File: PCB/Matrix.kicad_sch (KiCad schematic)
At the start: 67 parts, among them SW1 CPG151101S11, SW10 CPG151101S11, SW11 CPG151101S11, SW12 CPG151101S11, SW13 CPG151101S11, SW14 CPG151101S11, SW15 CPG151101S11, SW16 CPG151101S11, SW17 CPG151101S11, SW18 CPG151101S11, SW19 CPG151101S11, SW2 CPG151101S11, SW20 CPG151101S11, SW21 CPG151101S11, SW22 CPG151101S11, SW23 CPG151101S11, SW24 CPG151101S11, SW25 CPG151101S11, SW26 CPG151101S11, SW27 CPG151101S11, SW28 CPG151101S11, SW29 CPG151101S11, SW3 CPG151101S11, SW30 CPG151101S11, SW31 Encoder, SW4 CPG151101S11, SW5 CPG151101S11, SW6 CPG151101S11, SW7 CPG151101S11, SW8 CPG151101S11, SW9 CPG151101S11

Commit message: More routing
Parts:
- SW1, SW10, SW11, SW12, SW13, SW14, SW15, SW16, SW17, SW18, SW19, SW2, SW20, SW21, SW22, SW23, SW24, SW25, SW26, SW27, SW28, SW29, SW3, SW30, SW4, SW5, SW6, SW7, SW8, SW9: footprint Cantaloupe:MX_1U-Hotswap-Dual -> Cantaloupe:MX_1U-Hotswap-Flippable
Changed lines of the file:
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@@
       (effects (font (size 1.524 1.524)) hide)
     )
-    (property "Footprint" "Cantaloupe:MX_1U-Hotswap-Dual" (at 66.04 77.47 0)
+    (property "Footprint" "Cantaloupe:MX_1U-Hotswap-Flippable" (at 66.04 77.47 0)
       (effects (font (size 1.524 1.524)) hide)
     )
@@
       (effects (font (size 1.524 1.524)) hide)
     )
-    (property "Footprint" "Cantaloupe:MX_1U-Hotswap-Dual" (at 66.04 46.99 0)
+    (property "Footprint" "Cantaloupe:MX_1U-Hotswap-Flippable" (at 66.04 46.99 0)
       (effects (font (size 1.524 1.524)) hide)
     )
@@
       (effects (font (size 1.524 1.524)) hide)
     )
-    (property "Footprint" "Cantaloupe:MX_1U-Hotswap-Dual" (at 40.64 31.75 0)
+    (property "Footprint" "Cantaloupe:MX_1U-Hotswap-Flippable" (at 40.64 31.75 0)
       (effects (font (size 1.524 1.524)) hide)
     )
@@
       (effects (font (size 1.524 1.524)) hide)
     )
-    (property "Footprint" "Cantaloupe:MX_1U-Hotswap-Dual" (at 27.94 77.47 0)
+    (property "Footprint" "Cantaloupe:MX_1U-Hotswap-Flippable" (at 27.94 77.47 0)
       (effects (font (size 1.524 1.524)) hide)
     )
@@
       (effects (font (size 1.524 1.524)) hide)
     )
-    (property "Footprint" "Cantaloupe:MX_1U-Hotswap-Dual" (at 53.34 62.23 0)
+    (property "Footprint" "Cantaloupe:MX_1U-Hotswap-Flippable" (at 53.34 62.23 0)
       (effects (font (size 1.524 1.524)) hide)
     )
@@
       (effects (font (size 1.524 1.524)) hide)
     )
-    (property "Footprint" "Cantaloupe:MX_1U-Hotswap-Dual" (at 27.94 31.75 0)
+    (property "Footprint" "Cantaloupe:MX_1U-Hotswap-Flippable" (at 27.94 31.75 0)
       (effects (font (size 1.524 1.524)) hide)
     )
@@
       (effects (font (size 1.524 1.524)) hide)
     )
-    (property "Footprint" "Cantaloupe:MX_1U-Hotswap-Dual" (at 40.64 46.99 0)
+    (property "Footprint" "Cantaloupe:MX_1U-Hotswap-Flippable" (at 40.64 46.99 0)
       (effects (font (size 1.524 1.524)) hide)
     )
@@
       (effects (font (size 1.524 1.524)) hide)
     )
-    (property "Footprint" "Cantaloupe:MX_1U-Hotswap-Dual" (at 40.64 62.23 0)
+    (property "Footprint" "Cantaloupe:MX_1U-Hotswap-Flippable" (at 40.64 62.23 0)
       (effects (font (size 1.524 1.524)) hide)
     )
@@
       (effects (font (size 1.524 1.524)) hide)
     )
-    (property "Footprint" "Cantaloupe:MX_1U-Hotswap-Dual" (at 91.44 46.99 0)
+    (property "Footprint" "Cantaloupe:MX_1U-Hotswap-Flippable" (at 91.44 46.99 0)
       (effects (font (size 1.524 1.524)) hide)
     )
@@
       (effects (font (size 1.524 1.524)) hide)
     )
-    (property "Footprint" "Cantaloupe:MX_1U-Hotswap-Dual" (at 53.34 16.51 0)
+    (property "Footprint" "Cantaloupe:MX_1U-Hotswap-Flippable" (at 53.34 16.51 0)
       (effects (font (size 1.524 1.524)) hide)
     )
@@
       (effects (font (size 1.524 1.524)) hide)
     )
-    (property "Footprint" "Cantaloupe:MX_1U-Hotswap-Dual" (at 27.94 16.51 0)
+    (property "Footprint" "Cantaloupe:MX_1U-Hotswap-Flippable" (at 27.94 16.51 0)
       (effects (font (size 1.524 1.524)) hide)
     )
@@
       (effects (font (size 1.524 1.524)) hide)
     )
-    (property "Footprint" "Cantaloupe:MX_1U-Hotswap-Dual" (at 53.34 46.99 0)
+    (property "Footprint" "Cantaloupe:MX_1U-Hotswap-Flippable" (at 53.34 46.99 0)
       (effects (font (size 1.524 1.524)) hide)
     )
@@
       (effects (font (size 1.524 1.524)) hide)
     )
-    (property "Footprint" "Cantaloupe:MX_1U-Hotswap-Dual" (at 66.04 31.75 0)
+    (property "Footprint" "Cantaloupe:MX_1U-Hotswap-Flippable" (at 66.04 31.75 0)
       (effects (font (size 1.524 1.524)) hide)
     )
@@
       (effects (font (size 1.524 1.524)) hide)
     )
-    (property "Footprint" "Cantaloupe:MX_1U-Hotswap-Dual" (at 78.74 46.99 0)
+    (property "Footprint" "Cantaloupe:MX_1U-Hotswap-Flippable" (at 78.74 46.99 0)
       (effects (font (size 1.524 1.524)) hide)
     )
@@
       (effects (font (size 1.524 1.524)) hide)
     )
-    (property "Footprint" "Cantaloupe:MX_1U-Hotswap-Dual" (at 78.74 77.47 0)
+    (property "Footprint" "Cantaloupe:MX_1U-Hotswap-Flippable" (at 78.74 77.47 0)
       (effects (font (size 1.524 1.524)) hide)
     )
@@
       (effects (font (size 1.524 1.524)) hide)
     )
-    (property "Footprint" "Cantaloupe:MX_1U-Hotswap-Dual" (at 53.34 31.75 0)
+    (property "Footprint" "Cantaloupe:MX_1U-Hotswap-Flippable" (at 53.34 31.75 0)
       (effects (font (size 1.524 1.524)) hide)
     )
@@
       (effects (font (size 1.524 1.524)) hide)
     )
-    (property "Footprint" "Cantaloupe:MX_1U-Hotswap-Dual" (at 91.44 31.75 0)
+    (property "Footprint" "Cantaloupe:MX_1U-Hotswap-Flippable" (at 91.44 31.75 0)
       (effects (font (size 1.524 1.524)) hide)
     )
@@
       (effects (font (size 1.524 1.524)) hide)
     )
-    (property "Footprint" "Cantaloupe:MX_1U-Hotswap-Dual" (at 66.04 62.23 0)
+    (property "Footprint" "Cantaloupe:MX_1U-Hotswap-Flippable" (at 66.04 62.23 0)
       (effects (font (size 1.524 1.524)) hide)
     )
@@
       (effects (font (size 1.524 1.524)) hide)
     )
-    (property "Footprint" "Cantaloupe:MX_1U-Hotswap-Dual" (at 27.94 46.99 0)
+    (property "Footprint" "Cantaloupe:MX_1U-Hotswap-Flippable" (at 27.94 46.99 0)
       (effects (font (size 1.524 1.524)) hide)
     )
@@
       (effects (font (size 1.524 1.524)) hide)
     )
-    (property "Footprint" "Cantaloupe:MX_1U-Hotswap-Dual" (at 40.64 16.51 0)
+    (property "Footprint" "Cantaloupe:MX_1U-Hotswap-Flippable" (at 40.64 16.51 0)
       (effects (font (size 1.524 1.524)) hide)
     )
@@
       (effects (font (size 1.524 1.524)) hide)
     )
-    (property "Footprint" "Cantaloupe:MX_1U-Hotswap-Dual" (at 53.34 77.47 0)
+    (property "Footprint" "Cantaloupe:MX_1U-Hotswap-Flippable" (at 53.34 77.47 0)
       (effects (font (size 1.524 1.524)) hide)
     )
@@
       (effects (font (size 1.524 1.524)) hide)
     )
-    (property "Footprint" "Cantaloupe:MX_1U-Hotswap-Dual" (at 78.74 31.75 0)
+    (property "Footprint" "Cantaloupe:MX_1U-Hotswap-Flippable" (at 78.74 31.75 0)
       (effects (font (size 1.524 1.524)) hide)
     )
@@
       (effects (font (size 1.524 1.524)) hide)
     )
-    (property "Footprint" "Cantaloupe:MX_1U-Hotswap-Dual" (at 78.74 62.23 0)
+    (property "Footprint" "Cantaloupe:MX_1U-Hotswap-Flippable" (at 78.74 62.23 0)
       (effects (font (size 1.524 1.524)) hide)
     )
@@
       (effects (font (size 1.524 1.524)) hide)
     )
-    (property "Footprint" "Cantaloupe:MX_1U-Hotswap-Dual" (at 27.94 62.23 0)
+    (property "Footprint" "Cantaloupe:MX_1U-Hotswap-Flippable" (at 27.94 62.23 0)
       (effects (font (size 1.524 1.524)) hide)
     )
@@
       (effects (font (size 1.524 1.524)) hide)
     )
-    (property "Footprint" "Cantaloupe:MX_1U-Hotswap-Dual" (at 91.44 62.23 0)
+    (property "Footprint" "Cantaloupe:MX_1U-Hotswap-Flippable" (at 91.44 62.23 0)
       (effects (font (size 1.524 1.524)) hide)
     )
@@
       (effects (font (size 1.524 1.524)) hide)
     )
-    (property "Footprint" "Cantaloupe:MX_1U-Hotswap-Dual" (at 91.44 77.47 0)
+    (property "Footprint" "Cantaloupe:MX_1U-Hotswap-Flippable" (at 91.44 77.47 0)
       (effects (font (size 1.524 1.524)) hide)
     )
@@
       (effects (font (size 1.524 1.524)) hide)
     )
-    (property "Footprint" "Cantaloupe:MX_1U-Hotswap-Dual" (at 78.74 16.51 0)
+    (property "Footprint" "Cantaloupe:MX_1U-Hotswap-Flippable" (at 78.74 16.51 0)
       (effects (font (size 1.524 1.524)) hide)
     )
@@
       (effects (font (size 1.524 1.524)) hide)
     )
-    (property "Footprint" "Cantaloupe:MX_1U-Hotswap-Dual" (at 40.64 77.47 0)
+    (property "Footprint" "Cantaloupe:MX_1U-Hotswap-Flippable" (at 40.64 77.47 0)
       (effects (font (size 1.524 1.524)) hide)
     )
@@
       (effects (font (size 1.524 1.524)) hide)
     )
-    (property "Footprint" "Cantaloupe:MX_1U-Hotswap-Dual" (at 66.04 16.51 0)
+    (property "Footprint" "Cantaloupe:MX_1U-Hotswap-Flippable" (at 66.04 16.51 0)
       (effects (font (size 1.524 1.524)) hide)
     )
@@
       (effects (font (size 1.524 1.524)) hide)
     )
-    (property "Footprint" "Cantaloupe:MX_1U-Hotswap-Dual" (at 91.44 16.51 0)
-      (effects (font (size 1.524 1.524)) hide)
-    )
+    (property "Footprint" "Cantaloupe:MX_1U-Hotswap-Flippable" (at 91.44 16.51 0)
+      (effects (font (size 1.524 1.524)) hide)
+    )

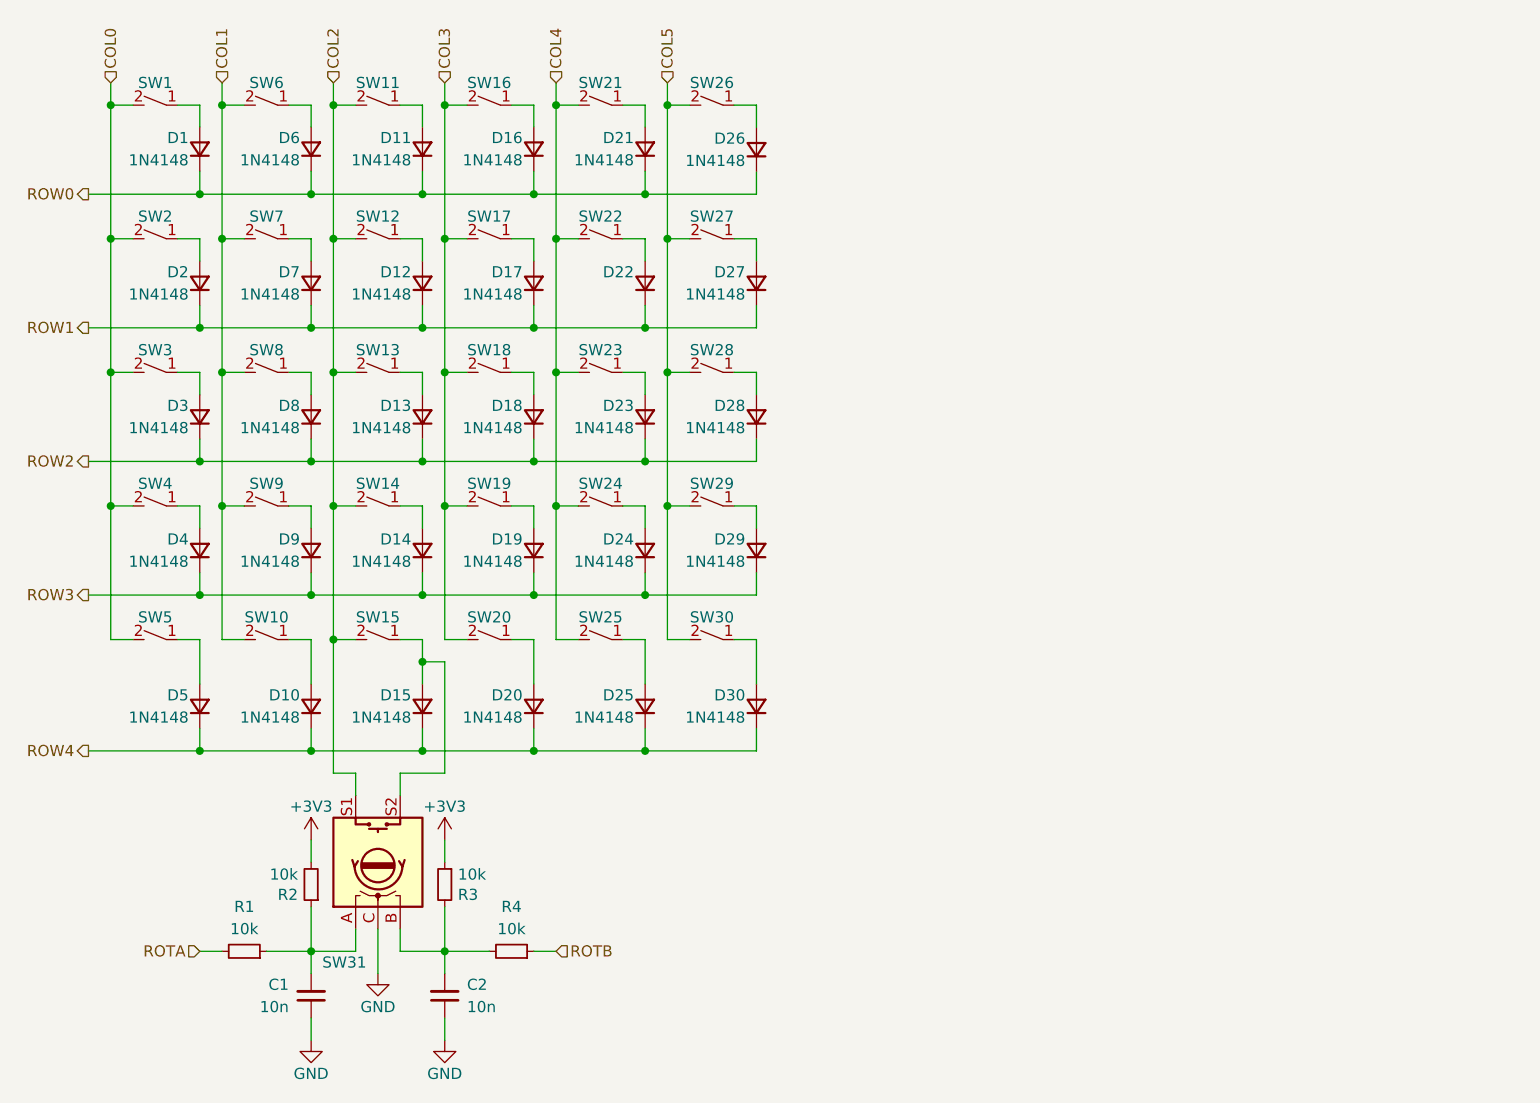
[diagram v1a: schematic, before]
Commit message: 08/08/2023 update
Removed Ogen footprint, and future VIK support is planned. Rerouted board following latest Honeydew revision. WIP support for the USB2541 is added, but it's very tentative and not yet complete. Added CX70M-24P1 footprint.
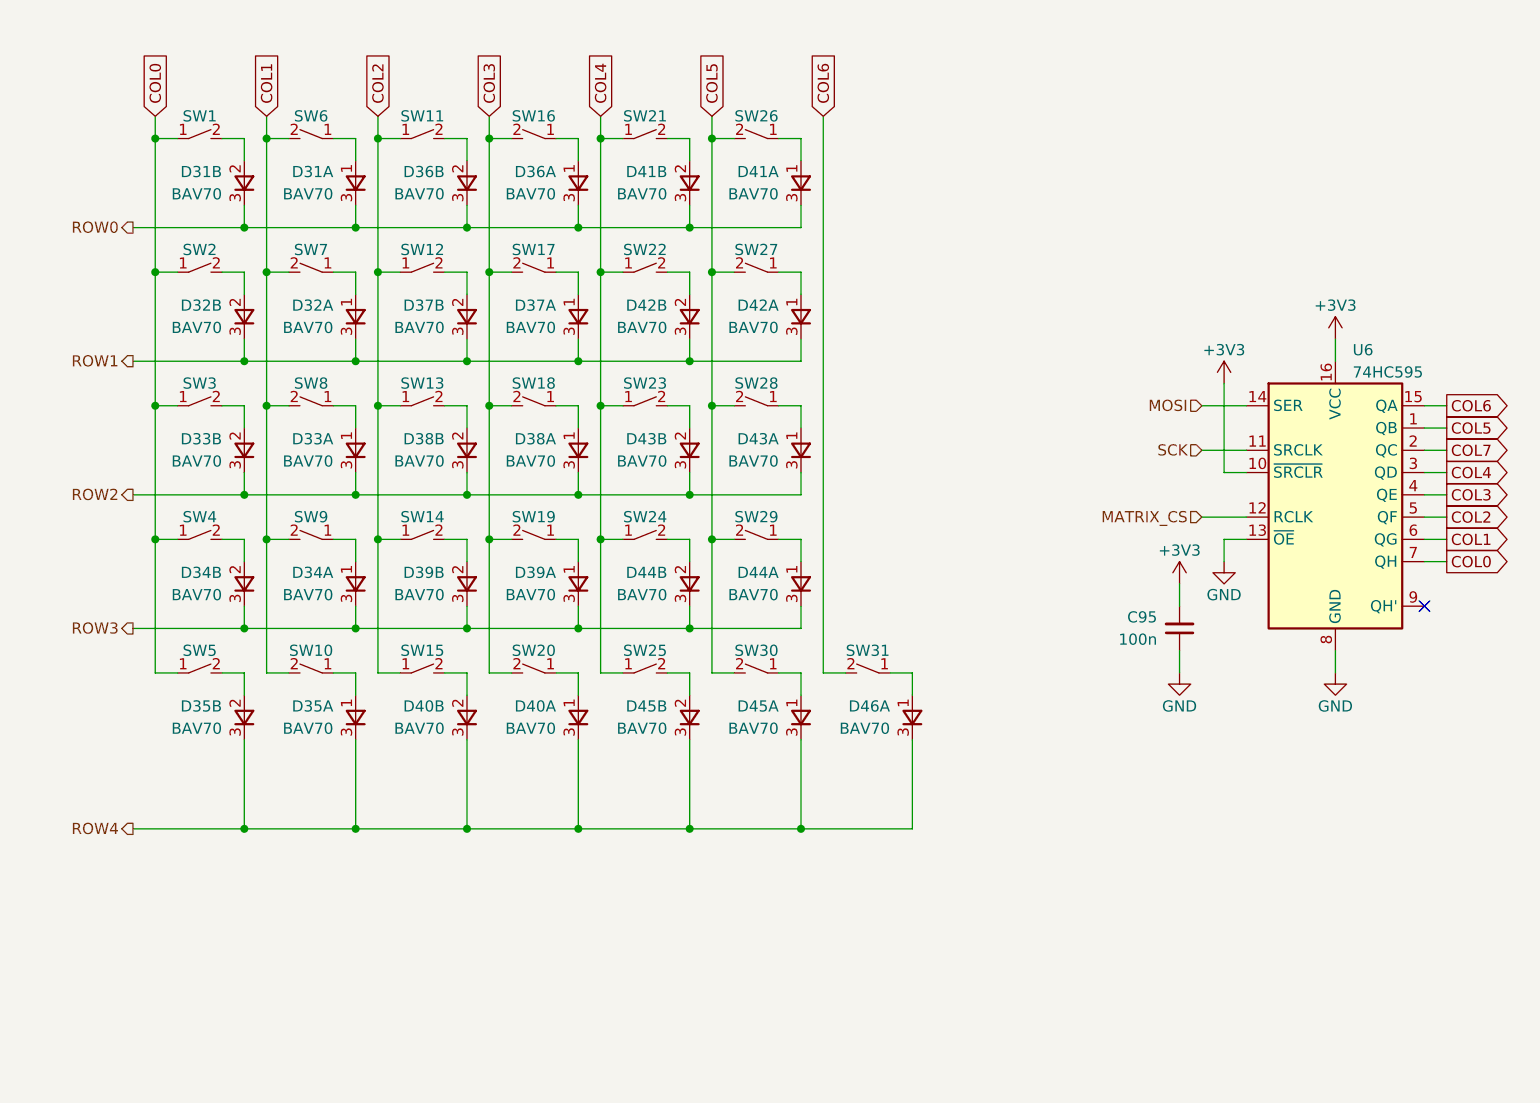
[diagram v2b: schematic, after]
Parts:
- removed C1, C2: 10n, Capacitor_SMD:C_0402_1005Metric, symbol Device:C_Small
- removed D1, D10, D11, D12, D13, D14, D15, D16, D17, D18, D19, D2, D20, D21, D22, D23, D24, D25, D26, D27, D28, D29, D3, D30, D4, D5, D6, D7, D8, D9: 1N4148, Cantaloupe:D_SOD-323, symbol Device:D_Small
- removed R1, R2, R3, R4: 10k, Resistor_SMD:R_0402_1005Metric, symbol Device:R_Small
- removed SW31: Encoder, Cantaloupe:EC11_Flippable, symbol Device:Rotary_Encoder_Switch
- added C95: 100n, Capacitor_SMD:C_0402_1005Metric, symbol Device:C_Small
- added D31, D32, D33, D34, D35, D36, D37, D38, D39, D40, D41, D42, D43, D44, D45, D46: BAV70, Cantaloupe:SOT-23-3, symbol Honeydew:D_Dual_CommonCathode_AAK_Split_Small
- added SW31: CPG151101S11, Cantaloupe:MXOnly-1U-Hotswap-Flippable, symbol Cantaloupe:SW_SPST_Small
- added U6: 74HC595, Cantaloupe:SOIC-16_3.9x9.9mm_P1.27mm, symbol 74xx:74HC595
- SW1, SW10, SW11, SW12, SW13, SW14, SW15, SW16, SW17, SW18, SW19, SW2, SW20, SW21, SW22, SW23, SW24, SW25, SW26, SW27, SW28, SW29, SW3, SW30, SW4, SW5, SW6, SW7, SW8, SW9: footprint Cantaloupe:MX_1U-Hotswap-Flippable -> Cantaloupe:MXOnly-1U-Hotswap-Flippable; LCSC C5184526 -> (none)
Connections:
- net +3V3: now also C95.2, U6.10 (~{SRCLR}), U6.16 (VCC)
- net COL0: now also SW1.1 (A), SW2.1 (A), SW3.1 (A), SW4.1 (A), SW5.1 (A), U6.7 (QH); no longer SW1.2 (B), SW2.2 (B), SW3.2 (B), SW4.2 (B), SW5.2 (B)
- net COL1: now also U6.6 (QG)
- net COL2: now also SW11.1 (A), SW12.1 (A), SW13.1 (A), SW14.1 (A), SW15.1 (A), U6.5 (QF); no longer SW11.2 (B), SW12.2 (B), SW13.2 (B), SW14.2 (B), SW15.2 (B)
- net COL3: now also U6.4 (QE)
- net COL4: now also SW21.1 (A), SW22.1 (A), SW23.1 (A), SW24.1 (A), SW25.1 (A), U6.3 (QD); no longer SW21.2 (B), SW22.2 (B), SW23.2 (B), SW24.2 (B), SW25.2 (B)
- net COL5: now also U6.1 (QB)
- net GND: now also C95.1, U6.13 (~{OE}), U6.8 (GND)
- net ROW0: now also D31.3 (K), D31.3 (K), D36.3 (K), D36.3 (K), D41.3 (K), D41.3 (K)
- net ROW1: now also D32.3 (K), D32.3 (K), D37.3 (K), D37.3 (K), D42.3 (K), D42.3 (K)
- net ROW2: now also D33.3 (K), D33.3 (K), D38.3 (K), D38.3 (K), D43.3 (K), D43.3 (K)
- net ROW3: now also D34.3 (K), D34.3 (K), D39.3 (K), D39.3 (K), D44.3 (K), D44.3 (K)
- net ROW4: now also D35.3 (K), D35.3 (K), D40.3 (K), D40.3 (K), D45.3 (K), D45.3 (K), D46.3 (K)
- net at SW20.1 (A): now also D40.1 (A)
- net at SW18.1 (A): now also D38.1 (A)
- net at SW10.1 (A): now also D35.1 (A)
- net at SW7.1 (A): now also D32.1 (A)
- net at SW8.1 (A): now also D33.1 (A)
- net at SW9.1 (A): now also D34.1 (A)
- net at SW28.1 (A): now also D43.1 (A)
- net at SW17.1 (A): now also D37.1 (A)
- net at SW27.1 (A): now also D42.1 (A)
- net at SW19.1 (A): now also D39.1 (A)
- net at SW6.1 (A): now also D31.1 (A)
- net at SW29.1 (A): now also D44.1 (A)
- net at SW16.1 (A): now also D36.1 (A)
- net at SW30.1 (A): now also D45.1 (A)
- net at SW26.1 (A): now also D41.1 (A)
- new net: D42.2 (A), SW22.2 (B)
- new net: D39.2 (A), SW14.2 (B)
- new net: D31.2 (A), SW1.2 (B)
- new net: D36.2 (A), SW11.2 (B)
- new net: D35.2 (A), SW5.2 (B)
- new net: D43.2 (A), SW23.2 (B)
- new net: D33.2 (A), SW3.2 (B)
- new net: D46.1 (A), SW31.1 (A)
- new net: D41.2 (A), SW21.2 (B)
- new net: D32.2 (A), SW2.2 (B)
- new net: D44.2 (A), SW24.2 (B)
- new net: D34.2 (A), SW4.2 (B)
- new net: D40.2 (A), SW15.2 (B)
- new net: D37.2 (A), SW12.2 (B)
- new net: D38.2 (A), SW13.2 (B)
- new net: D45.2 (A), SW25.2 (B)
- new net COL6: SW31.2 (B), U6.15 (QA)
- new net COL7: U6.2 (QC)
- new net MATRIX_CS: U6.12 (RCLK)
- new net MOSI: U6.14 (SER)
- new net SCK: U6.11 (SRCLK)
- no-connect marks 0 -> 1
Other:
- company: (none) -> Created by Ariamelon (https://github.com/Ariamelon/Cantaloupe/)
- title: (none) -> Cantaloupe split ergonomic keyboard
